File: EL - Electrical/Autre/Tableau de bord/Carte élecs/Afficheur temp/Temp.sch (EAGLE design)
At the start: 25 parts, among them IC1 MCP23008P, IC2 MCP23008P, X1 22-23-2041

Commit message: MAJ plan afficheur temp
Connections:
- net GP10: now also R2B.2; no longer R1C.2
- net GP11: now also R2A.2; no longer R1G.2
- net GP12: now also R3AB.2; no longer R1D.2
- net GP13: now also R2F.2; no longer R1E.2
- net GP14: now also R2G.2; no longer R2DP.1
- net GP20: now also R1G.2; no longer R3AB.2
- net GP21: now also R1C.2; no longer R2F.2
- net GP22: now also R1D.2; no longer R2G.2
- net GP23: now also R1E.2; no longer R2A.2
- net GP24: now also R1F.2; no longer R2B.2
- net GP25: now also R1A.2; no longer R1F.2
- net GP26: now also R1B.2; no longer R1A.2
- net GP27: now also R2DP.1; no longer R1B.2
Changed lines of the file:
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@@
 </segment>
 <segment>
-<pinref part="R2DP" gate="G$1" pin="1"/>
-<wire x1="96.52" y1="109.22" x2="100.33" y2="109.22" width="0.1524" layer="91"/>
-<label x="100.33" y="109.22" size="1.778" layer="95" xref="yes"/>
+<pinref part="R2G" gate="G$1" pin="2"/>
+<wire x1="45.72" y1="109.22" x2="43.18" y2="109.22" width="0.1524" layer="91"/>
+<label x="43.18" y="109.22" size="1.778" layer="95" rot="R180" xref="yes"/>
 </segment>
 </net>
@@
 </segment>
 <segment>
-<pinref part="R1E" gate="G$1" pin="2"/>
-<wire x1="45.72" y1="142.24" x2="40.64" y2="142.24" width="0.1524" layer="91"/>
-<label x="40.64" y="142.24" size="1.778" layer="95" rot="R180" xref="yes"/>
+<pinref part="R2F" gate="G$1" pin="2"/>
+<wire x1="45.72" y1="111.76" x2="34.29" y2="111.76" width="0.1524" layer="91"/>
+<label x="34.29" y="111.76" size="1.778" layer="95" rot="R180" xref="yes"/>
 </segment>
 </net>
@@
 </segment>
 <segment>
-<pinref part="R1D" gate="G$1" pin="2"/>
-<wire x1="45.72" y1="144.78" x2="31.75" y2="144.78" width="0.1524" layer="91"/>
-<label x="31.75" y="144.78" size="1.778" layer="95" rot="R180" xref="yes"/>
+<pinref part="R3AB" gate="G$1" pin="2"/>
+<wire x1="95.25" y1="152.4" x2="93.98" y2="152.4" width="0.1524" layer="91"/>
+<label x="93.98" y="148.59" size="1.778" layer="95" rot="R180" xref="yes"/>
+<wire x1="93.98" y1="152.4" x2="93.98" y2="148.59" width="0.1524" layer="91"/>
 </segment>
 </net>
@@
 </segment>
 <segment>
-<pinref part="R1G" gate="G$1" pin="2"/>
-<wire x1="45.72" y1="137.16" x2="40.64" y2="137.16" width="0.1524" layer="91"/>
-<label x="40.64" y="137.16" size="1.778" layer="95" rot="R180" xref="yes"/>
+<pinref part="R2A" gate="G$1" pin="2"/>
+<wire x1="45.72" y1="124.46" x2="43.18" y2="124.46" width="0.1524" layer="91"/>
+<label x="43.18" y="124.46" size="1.778" layer="95" rot="R180" xref="yes"/>
 </segment>
 </net>
@@
 </segment>
 <segment>
-<pinref part="R1C" gate="G$1" pin="2"/>
-<wire x1="45.72" y1="147.32" x2="40.64" y2="147.32" width="0.1524" layer="91"/>
-<label x="40.64" y="147.32" size="1.778" layer="95" rot="R180" xref="yes"/>
+<pinref part="R2B" gate="G$1" pin="2"/>
+<wire x1="45.72" y1="121.92" x2="34.29" y2="121.92" width="0.1524" layer="91"/>
+<label x="34.29" y="121.92" size="1.778" layer="95" rot="R180" xref="yes"/>
 </segment>
 </net>
@@
 </segment>
 <segment>
-<pinref part="R1B" gate="G$1" pin="2"/>
-<wire x1="45.72" y1="149.86" x2="31.75" y2="149.86" width="0.1524" layer="91"/>
-<label x="31.75" y="149.86" size="1.778" layer="95" rot="R180" xref="yes"/>
+<pinref part="R2DP" gate="G$1" pin="1"/>
+<wire x1="96.52" y1="109.22" x2="100.33" y2="109.22" width="0.1524" layer="91"/>
+<label x="100.33" y="109.22" size="1.778" layer="95" xref="yes"/>
 </segment>
 </net>
@@
 </segment>
 <segment>
-<pinref part="R1A" gate="G$1" pin="2"/>
-<wire x1="45.72" y1="152.4" x2="40.64" y2="152.4" width="0.1524" layer="91"/>
-<label x="40.64" y="152.4" size="1.778" layer="95" rot="R180" xref="yes"/>
+<pinref part="R1B" gate="G$1" pin="2"/>
+<wire x1="45.72" y1="149.86" x2="31.75" y2="149.86" width="0.1524" layer="91"/>
+<label x="31.75" y="149.86" size="1.778" layer="95" rot="R180" xref="yes"/>
 </segment>
 </net>
@@
 </segment>
 <segment>
-<pinref part="R1F" gate="G$1" pin="2"/>
-<wire x1="45.72" y1="139.7" x2="31.75" y2="139.7" width="0.1524" layer="91"/>
-<label x="31.75" y="139.7" size="1.778" layer="95" rot="R180" xref="yes"/>
+<pinref part="R1A" gate="G$1" pin="2"/>
+<wire x1="45.72" y1="152.4" x2="40.64" y2="152.4" width="0.1524" layer="91"/>
+<label x="40.64" y="152.4" size="1.778" layer="95" rot="R180" xref="yes"/>
 </segment>
 </net>
@@
 </segment>
 <segment>
-<pinref part="R2B" gate="G$1" pin="2"/>
-<wire x1="45.72" y1="121.92" x2="34.29" y2="121.92" width="0.1524" layer="91"/>
-<label x="34.29" y="121.92" size="1.778" layer="95" rot="R180" xref="yes"/>
+<pinref part="R1F" gate="G$1" pin="2"/>
+<wire x1="45.72" y1="139.7" x2="31.75" y2="139.7" width="0.1524" layer="91"/>
+<label x="31.75" y="139.7" size="1.778" layer="95" rot="R180" xref="yes"/>
 </segment>
 </net>
@@
 </segment>
 <segment>
-<pinref part="R2A" gate="G$1" pin="2"/>
-<wire x1="45.72" y1="124.46" x2="43.18" y2="124.46" width="0.1524" layer="91"/>
-<label x="43.18" y="124.46" size="1.778" layer="95" rot="R180" xref="yes"/>
+<pinref part="R1E" gate="G$1" pin="2"/>
+<wire x1="45.72" y1="142.24" x2="40.64" y2="142.24" width="0.1524" layer="91"/>
+<label x="40.64" y="142.24" size="1.778" layer="95" rot="R180" xref="yes"/>
 </segment>
 </net>
@@
 </segment>
 <segment>
-<pinref part="R2G" gate="G$1" pin="2"/>
-<wire x1="45.72" y1="109.22" x2="43.18" y2="109.22" width="0.1524" layer="91"/>
-<label x="43.18" y="109.22" size="1.778" layer="95" rot="R180" xref="yes"/>
+<pinref part="R1D" gate="G$1" pin="2"/>
+<wire x1="45.72" y1="144.78" x2="31.75" y2="144.78" width="0.1524" layer="91"/>
+<label x="31.75" y="144.78" size="1.778" layer="95" rot="R180" xref="yes"/>
 </segment>
 </net>
@@
 </segment>
 <segment>
-<pinref part="R2F" gate="G$1" pin="2"/>
-<wire x1="45.72" y1="111.76" x2="34.29" y2="111.76" width="0.1524" layer="91"/>
-<label x="34.29" y="111.76" size="1.778" layer="95" rot="R180" xref="yes"/>
+<pinref part="R1C" gate="G$1" pin="2"/>
+<wire x1="45.72" y1="147.32" x2="40.64" y2="147.32" width="0.1524" layer="91"/>
+<label x="40.64" y="147.32" size="1.778" layer="95" rot="R180" xref="yes"/>
 </segment>
 </net>
@@
 </segment>
 <segment>
-<pinref part="R3AB" gate="G$1" pin="2"/>
-<wire x1="95.25" y1="152.4" x2="93.98" y2="152.4" width="0.1524" layer="91"/>
-<label x="93.98" y="148.59" size="1.778" layer="95" rot="R180" xref="yes"/>
-<wire x1="93.98" y1="152.4" x2="93.98" y2="148.59" width="0.1524" layer="91"/>
+<pinref part="R1G" gate="G$1" pin="2"/>
+<wire x1="45.72" y1="137.16" x2="40.64" y2="137.16" width="0.1524" layer="91"/>
+<label x="40.64" y="137.16" size="1.778" layer="95" rot="R180" xref="yes"/>
 </segment>
 </net>

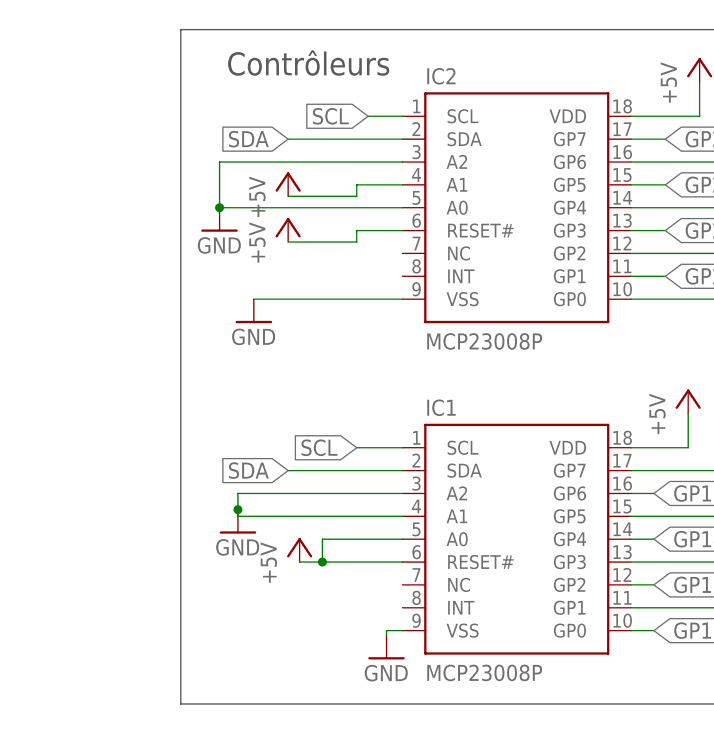
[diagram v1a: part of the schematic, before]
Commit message: changement d'adresse afficheur temp
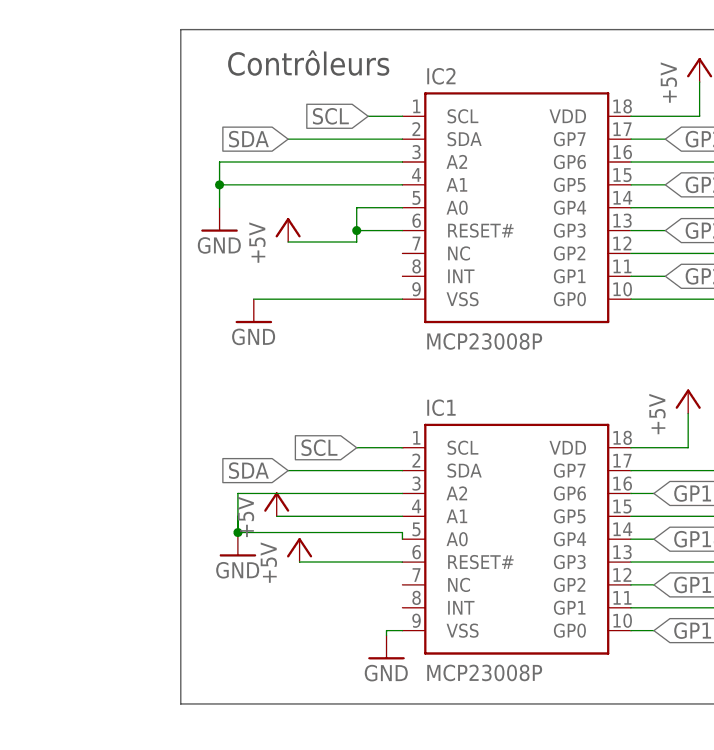
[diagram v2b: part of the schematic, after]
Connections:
- net +5V: now also IC1.A1, IC2.A0; no longer IC1.A0, IC2.A1
- net GND: now also IC1.A0, IC2.A1; no longer IC1.A1, IC2.A0
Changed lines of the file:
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@@
 <part name="IC2" library="microchip-dspic" deviceset="MCP23008" device="P"/>
 <part name="P+3" library="supply1" library_urn="urn:adsk.eagle:library:371" deviceset="+5V" device=""/>
-<part name="P+8" library="supply1" library_urn="urn:adsk.eagle:library:371" deviceset="+5V" device=""/>
 <part name="GND6" library="supply1" library_urn="urn:adsk.eagle:library:371" deviceset="GND" device=""/>
 <part name="GND7" library="supply1" library_urn="urn:adsk.eagle:library:371" deviceset="GND" device=""/>
@@
 <part name="P+11" library="supply1" library_urn="urn:adsk.eagle:library:371" deviceset="+5V" device=""/>
 <part name="R3AB" library="rcl" library_urn="urn:adsk.eagle:library:334" deviceset="R-EU_" device="0204/7" package3d_urn="urn:adsk.eagle:package:23498/1" value="470"/>
+<part name="P+12" library="supply1" library_urn="urn:adsk.eagle:library:371" deviceset="+5V" device=""/>
 </parts>
 <sheets>
@@
 <attribute name="VALUE" x="56.65" y="15.98" size="1.778" layer="96"/>
 </instance>
-<instance part="GND3" gate="1" x="42.68" y="32.49" smashed="yes">
-<attribute name="VALUE" x="40.14" y="29.95" size="1.778" layer="96"/>
+<instance part="GND3" gate="1" x="42.68" y="29.95" smashed="yes">
+<attribute name="VALUE" x="40.14" y="27.41" size="1.778" layer="96"/>
 </instance>
 <instance part="P+1" gate="1" x="212.28" y="61.41" smashed="yes">
@@
 <attribute name="VALUE" x="91.44" y="80.01" size="1.778" layer="96" rot="R90"/>
 </instance>
-<instance part="P+8" gate="1" x="48.26" y="72.39" smashed="yes">
-<attribute name="VALUE" x="45.72" y="67.31" size="1.778" layer="96" rot="R90"/>
-</instance>
 <instance part="GND6" gate="1" x="44.45" y="55.88" smashed="yes">
 <attribute name="VALUE" x="41.91" y="53.34" size="1.778" layer="96"/>
@@
 <attribute name="NAME" x="108.22" y="154.4814" size="1.778" layer="95" rot="R180"/>
 <attribute name="VALUE" x="97.64" y="154.702" size="1.778" layer="96" rot="R180"/>
+</instance>
+<instance part="P+12" gate="1" x="46.99" y="36.83" smashed="yes">
+<attribute name="VALUE" x="44.45" y="31.75" size="1.778" layer="96" rot="R90"/>
 </instance>
 </instances>
@@
 <pinref part="GND3" gate="1" pin="GND"/>
 <wire x1="60.96" y1="36.83" x2="42.68" y2="36.83" width="0.1524" layer="91"/>
-<wire x1="42.68" y1="36.83" x2="42.68" y2="35.03" width="0.1524" layer="91"/>
-<pinref part="IC1" gate="A" pin="A1"/>
-<wire x1="60.96" y1="34.29" x2="42.68" y2="34.29" width="0.1524" layer="91"/>
-<wire x1="42.68" y1="34.29" x2="42.68" y2="35.03" width="0.1524" layer="91"/>
-<junction x="42.68" y="35.03"/>
+<wire x1="42.68" y1="36.83" x2="42.68" y2="32.49" width="0.1524" layer="91"/>
+<wire x1="42.68" y1="34.29" x2="42.68" y2="32.49" width="0.1524" layer="91"/>
+<junction x="42.68" y="32.49"/>
+<pinref part="IC1" gate="A" pin="A0"/>
+<wire x1="60.96" y1="31.75" x2="60.96" y2="32.49" width="0.1524" layer="91"/>
+<wire x1="60.96" y1="32.49" x2="42.68" y2="32.49" width="0.1524" layer="91"/>
 </segment>
 <segment>
@@
 <segment>
 <pinref part="GND7" gate="1" pin="GND"/>
-<pinref part="IC2" gate="A" pin="A0"/>
 <pinref part="IC2" gate="A" pin="A2"/>
-<wire x1="40.64" y1="68.58" x2="60.96" y2="68.58" width="0.1524" layer="91"/>
 <wire x1="60.96" y1="73.66" x2="40.64" y2="73.66" width="0.1524" layer="91"/>
-<wire x1="40.64" y1="73.66" x2="40.64" y2="68.58" width="0.1524" layer="91"/>
-<junction x="40.64" y="68.58"/>
+<wire x1="40.64" y1="73.66" x2="40.64" y2="71.12" width="0.1524" layer="91"/>
+<pinref part="IC2" gate="A" pin="A1"/>
+<wire x1="40.64" y1="71.12" x2="40.64" y2="68.58" width="0.1524" layer="91"/>
+<wire x1="60.96" y1="71.12" x2="40.64" y2="71.12" width="0.1524" layer="91"/>
+<junction x="40.64" y="71.12"/>
 </segment>
 </net>
@@
 </segment>
 <segment>
-<pinref part="IC1" gate="A" pin="A0"/>
-<wire x1="60.96" y1="31.75" x2="52.07" y2="31.75" width="0.1524" layer="91"/>
-<wire x1="52.07" y1="31.75" x2="52.07" y2="29.21" width="0.1524" layer="91"/>
 <pinref part="P+5" gate="1" pin="+5V"/>
-<wire x1="52.07" y1="29.21" x2="49.53" y2="29.21" width="0.1524" layer="91"/>
 <pinref part="IC1" gate="A" pin="RESET#"/>
-<wire x1="60.96" y1="29.21" x2="52.07" y2="29.21" width="0.1524" layer="91"/>
-<junction x="52.07" y="29.21"/>
+<wire x1="60.96" y1="29.21" x2="49.53" y2="29.21" width="0.1524" layer="91"/>
 </segment>
 <segment>
@@
 <pinref part="IC2" gate="A" pin="RESET#"/>
 <wire x1="55.88" y1="66.04" x2="60.96" y2="66.04" width="0.1524" layer="91"/>
+<pinref part="IC2" gate="A" pin="A0"/>
+<wire x1="60.96" y1="68.58" x2="55.88" y2="68.58" width="0.1524" layer="91"/>
+<wire x1="55.88" y1="68.58" x2="55.88" y2="66.04" width="0.1524" layer="91"/>
+<junction x="55.88" y="66.04"/>
 </segment>
 <segment>
@@
 <wire x1="86.36" y1="78.74" x2="93.98" y2="78.74" width="0.1524" layer="91"/>
 <wire x1="93.98" y1="78.74" x2="93.98" y2="82.55" width="0.1524" layer="91"/>
-</segment>
-<segment>
-<pinref part="P+8" gate="1" pin="+5V"/>
-<wire x1="48.26" y1="69.85" x2="55.88" y2="69.85" width="0.1524" layer="91"/>
-<wire x1="55.88" y1="69.85" x2="55.88" y2="71.12" width="0.1524" layer="91"/>
-<pinref part="IC2" gate="A" pin="A1"/>
-<wire x1="55.88" y1="71.12" x2="60.96" y2="71.12" width="0.1524" layer="91"/>
 </segment>
 <segment>
@@
 <junction x="134.62" y="152.4"/>
 </segment>
+<segment>
+<pinref part="P+12" gate="1" pin="+5V"/>
+<pinref part="IC1" gate="A" pin="A1"/>
+<wire x1="46.99" y1="34.29" x2="60.96" y2="34.29" width="0.1524" layer="91"/>
+</segment>
 </net>

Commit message: légère modifs à terminer
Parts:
- added R3AB1: 230, rcl:R-EU_0204/7
- R3AB: value 470 -> 230
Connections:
- new net N$16: LED2DIG1.B, R3AB1.1
- net GP12: now also R3AB1.2
- net N$17: no longer LED2DIG1.B
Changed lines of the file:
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@@
 <part name="R2DP" library="rcl" library_urn="urn:adsk.eagle:library:334" deviceset="R-EU_" device="0204/7" package3d_urn="urn:adsk.eagle:package:23498/1" value="470"/>
 <part name="P+11" library="supply1" library_urn="urn:adsk.eagle:library:371" deviceset="+5V" device=""/>
-<part name="R3AB" library="rcl" library_urn="urn:adsk.eagle:library:334" deviceset="R-EU_" device="0204/7" package3d_urn="urn:adsk.eagle:package:23498/1" value="470"/>
+<part name="R3AB" library="rcl" library_urn="urn:adsk.eagle:library:334" deviceset="R-EU_" device="0204/7" package3d_urn="urn:adsk.eagle:package:23498/1" value="230"/>
 <part name="P+12" library="supply1" library_urn="urn:adsk.eagle:library:371" deviceset="+5V" device=""/>
+<part name="R3AB1" library="rcl" library_urn="urn:adsk.eagle:library:334" deviceset="R-EU_" device="0204/7" package3d_urn="urn:adsk.eagle:package:23498/1" value="230"/>
 </parts>
 <sheets>
@@
 <attribute name="VALUE" x="44.45" y="31.75" size="1.778" layer="96" rot="R90"/>
 </instance>
+<instance part="R3AB1" gate="G$1" x="100.33" y="149.86" smashed="yes" rot="R180">
+<attribute name="NAME" x="108.22" y="151.9414" size="1.778" layer="95" rot="R180"/>
+<attribute name="VALUE" x="97.64" y="152.162" size="1.778" layer="96" rot="R180"/>
+</instance>
 </instances>
 <busses>
@@
 <wire x1="95.25" y1="152.4" x2="93.98" y2="152.4" width="0.1524" layer="91"/>
 <label x="93.98" y="148.59" size="1.778" layer="95" rot="R180" xref="yes"/>
-<wire x1="93.98" y1="152.4" x2="93.98" y2="148.59" width="0.1524" layer="91"/>
+<wire x1="93.98" y1="152.4" x2="93.98" y2="149.86" width="0.1524" layer="91"/>
+<pinref part="R3AB1" gate="G$1" pin="2"/>
+<wire x1="93.98" y1="149.86" x2="93.98" y2="148.59" width="0.1524" layer="91"/>
+<wire x1="95.25" y1="149.86" x2="93.98" y2="149.86" width="0.1524" layer="91"/>
+<junction x="93.98" y="149.86"/>
 </segment>
 </net>
@@
 <pinref part="LED2" gate="DIG1" pin="A"/>
 <wire x1="105.41" y1="152.4" x2="107.95" y2="152.4" width="0.1524" layer="91"/>
+</segment>
+</net>
+<net name="N$16" class="0">
+<segment>
 <pinref part="LED2" gate="DIG1" pin="B"/>
 <wire x1="107.95" y1="149.86" x2="105.41" y2="149.86" width="0.1524" layer="91"/>
-<wire x1="105.41" y1="149.86" x2="105.41" y2="152.4" width="0.1524" layer="91"/>
-<junction x="105.41" y="152.4"/>
-</segment>
-</net>
+<pinref part="R3AB1" gate="G$1" pin="1"/>
+</segment>
+</net>

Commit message: fin des carte tdb
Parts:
- removed R3AB, R3AB1: 230, rcl:R-EU_0204/7
- added R3A, R3B: 230, rcl:R-EU_0204/7
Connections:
- net GP12: now also R3A.2, R3B.2; no longer R3AB.2, R3AB1.2
- net N$16: now also R3B.1; no longer R3AB1.1
- net N$17: now also R3A.1; no longer R3AB.1
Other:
- note added: "Afficheur Temp v1.0"
- note removed: "Afficheur Temp V1.0"
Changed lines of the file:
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@@
 <part name="R2DP" library="rcl" library_urn="urn:adsk.eagle:library:334" deviceset="R-EU_" device="0204/7" package3d_urn="urn:adsk.eagle:package:23498/1" value="470"/>
 <part name="P+11" library="supply1" library_urn="urn:adsk.eagle:library:371" deviceset="+5V" device=""/>
-<part name="R3AB" library="rcl" library_urn="urn:adsk.eagle:library:334" deviceset="R-EU_" device="0204/7" package3d_urn="urn:adsk.eagle:package:23498/1" value="230"/>
+<part name="R3A" library="rcl" library_urn="urn:adsk.eagle:library:334" deviceset="R-EU_" device="0204/7" package3d_urn="urn:adsk.eagle:package:23498/1" value="230"/>
 <part name="P+12" library="supply1" library_urn="urn:adsk.eagle:library:371" deviceset="+5V" device=""/>
-<part name="R3AB1" library="rcl" library_urn="urn:adsk.eagle:library:334" deviceset="R-EU_" device="0204/7" package3d_urn="urn:adsk.eagle:package:23498/1" value="230"/>
+<part name="R3B" library="rcl" library_urn="urn:adsk.eagle:library:334" deviceset="R-EU_" device="0204/7" package3d_urn="urn:adsk.eagle:package:23498/1" value="230"/>
 </parts>
 <sheets>
@@
 <plain>
 <text x="167.14" y="9.16" size="5.08" layer="94">Afficheur
-Temp V1.0</text>
+Temp v1.0</text>
 <text x="216.44" y="20.32" size="2.54" layer="94">EPSA Saison 2018/2019</text>
 <wire x1="180.8" y1="166.26" x2="180.8" y2="95.14" width="0.1524" layer="97"/>
@@
 <attribute name="VALUE" x="132.08" y="153.67" size="1.778" layer="96" rot="R90"/>
 </instance>
-<instance part="R3AB" gate="G$1" x="100.33" y="152.4" smashed="yes" rot="R180">
-<attribute name="NAME" x="108.22" y="154.4814" size="1.778" layer="95" rot="R180"/>
-<attribute name="VALUE" x="97.64" y="154.702" size="1.778" layer="96" rot="R180"/>
-</instance>
-<instance part="P+12" gate="1" x="46.99" y="36.83" smashed="yes">
-<attribute name="VALUE" x="44.45" y="31.75" size="1.778" layer="96" rot="R90"/>
-</instance>
-<instance part="R3AB1" gate="G$1" x="100.33" y="149.86" smashed="yes" rot="R180">
-<attribute name="NAME" x="108.22" y="151.9414" size="1.778" layer="95" rot="R180"/>
-<attribute name="VALUE" x="97.64" y="152.162" size="1.778" layer="96" rot="R180"/>
+<instance part="R3A" gate="G$1" x="97.79" y="152.4" smashed="yes" rot="R180">
+<attribute name="NAME" x="105.68" y="154.4814" size="1.778" layer="95" rot="R180"/>
+<attribute name="VALUE" x="95.1" y="154.702" size="1.778" layer="96" rot="R180"/>
+</instance>
+<instance part="P+12" gate="1" x="52.07" y="36.83" smashed="yes">
+<attribute name="VALUE" x="49.53" y="31.75" size="1.778" layer="96" rot="R90"/>
+</instance>
+<instance part="R3B" gate="G$1" x="97.79" y="149.86" smashed="yes" rot="R180">
+<attribute name="NAME" x="105.68" y="151.9414" size="1.778" layer="95" rot="R180"/>
+<attribute name="VALUE" x="95.1" y="152.162" size="1.778" layer="96" rot="R180"/>
 </instance>
 </instances>
@@
 <pinref part="P+12" gate="1" pin="+5V"/>
 <pinref part="IC1" gate="A" pin="A1"/>
-<wire x1="46.99" y1="34.29" x2="60.96" y2="34.29" width="0.1524" layer="91"/>
+<wire x1="52.07" y1="34.29" x2="60.96" y2="34.29" width="0.1524" layer="91"/>
 </segment>
 </net>
@@
 </segment>
 <segment>
-<pinref part="R3AB" gate="G$1" pin="2"/>
-<wire x1="95.25" y1="152.4" x2="93.98" y2="152.4" width="0.1524" layer="91"/>
-<label x="93.98" y="148.59" size="1.778" layer="95" rot="R180" xref="yes"/>
-<wire x1="93.98" y1="152.4" x2="93.98" y2="149.86" width="0.1524" layer="91"/>
-<pinref part="R3AB1" gate="G$1" pin="2"/>
-<wire x1="93.98" y1="149.86" x2="93.98" y2="148.59" width="0.1524" layer="91"/>
-<wire x1="95.25" y1="149.86" x2="93.98" y2="149.86" width="0.1524" layer="91"/>
-<junction x="93.98" y="149.86"/>
+<pinref part="R3A" gate="G$1" pin="2"/>
+<wire x1="92.71" y1="152.4" x2="88.9" y2="152.4" width="0.1524" layer="91"/>
+<label x="88.9" y="147.32" size="1.778" layer="95" rot="R270" xref="yes"/>
+<wire x1="88.9" y1="152.4" x2="88.9" y2="149.86" width="0.1524" layer="91"/>
+<pinref part="R3B" gate="G$1" pin="2"/>
+<wire x1="88.9" y1="149.86" x2="88.9" y2="147.32" width="0.1524" layer="91"/>
+<wire x1="92.71" y1="149.86" x2="88.9" y2="149.86" width="0.1524" layer="91"/>
+<junction x="88.9" y="149.86"/>
 </segment>
 </net>
@@
 <net name="N$17" class="0">
 <segment>
-<pinref part="R3AB" gate="G$1" pin="1"/>
+<pinref part="R3A" gate="G$1" pin="1"/>
 <pinref part="LED2" gate="DIG1" pin="A"/>
-<wire x1="105.41" y1="152.4" x2="107.95" y2="152.4" width="0.1524" layer="91"/>
+<wire x1="102.87" y1="152.4" x2="107.95" y2="152.4" width="0.1524" layer="91"/>
 </segment>
 </net>
@@
 <segment>
 <pinref part="LED2" gate="DIG1" pin="B"/>
-<wire x1="107.95" y1="149.86" x2="105.41" y2="149.86" width="0.1524" layer="91"/>
-<pinref part="R3AB1" gate="G$1" pin="1"/>
-</segment>
-</net>
+<wire x1="107.95" y1="149.86" x2="102.87" y2="149.86" width="0.1524" layer="91"/>
+<pinref part="R3B" gate="G$1" pin="1"/>
+</segment>
+</net>
